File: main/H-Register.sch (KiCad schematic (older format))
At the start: 19 parts, among them U74 74LS245, U75 74LS173, U76 74LS173

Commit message: Replot main with symbols
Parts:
- renumbered D54 to D46, D55 to D47, D56 to D48, D57 to D49, D58 to D50, D59 to D51, D60 to D52, D61 to D53, R60 to R52, R61 to R53, R62 to R54, R63 to R55, R64 to R56, R65 to R57, R66 to R58, R67 to R59, U74 to U59, U75 to U60, U76 to U61
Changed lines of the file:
@@
 Sheet 16 26
 Title "H Register"
-Date "2019-11-13"
+Date "2019-11-17"
 Rev "v1.0"
 Comp "Christopher Milan"
@@
 AR Path="/5D9C73BD/5DA5FEC5" Ref="U?"  Part="1"
 AR Path="/5D9E8F33/5DA5FEC5" Ref="U?"  Part="1"
-AR Path="/5DA98D6D/5DA9A571/5DA5FEC5" Ref="U74"  Part="1"
-F 0 "U74" V 2996 2656 50  0000 R CNN
+AR Path="/5DA98D6D/5DA9A571/5DA5FEC5" Ref="U59"  Part="1"
+F 0 "U59" V 2996 2656 50  0000 R CNN
 F 1 "74LS245" V 2905 2656 50  0000 R CNN
 F 2 "" H 2950 3500 50  0001 C CNN
@@
 AR Path="/5D9C73BD/5DA5FEF2" Ref="U?"  Part="1"
 AR Path="/5D9E8F33/5DA5FEF2" Ref="U?"  Part="1"
-AR Path="/5DA98D6D/5DA9A571/5DA5FEF2" Ref="U76"  Part="1"
-F 0 "U76" V 7504 4444 50  0000 L CNN
+AR Path="/5DA98D6D/5DA9A571/5DA5FEF2" Ref="U61"  Part="1"
+F 0 "U61" V 7504 4444 50  0000 L CNN
 F 1 "74LS173" V 7595 4444 50  0000 L CNN
 F 2 "" H 7550 3500 50  0001 C CNN
@@
 AR Path="/5D9C73BD/5DA5FF1C" Ref="D?"  Part="1"
 AR Path="/5D9E8F33/5DA5FF1C" Ref="D?"  Part="1"
-AR Path="/5DA98D6D/5DA9A571/5DA5FF1C" Ref="D54"  Part="1"
-F 0 "D54" V 3539 5883 50  0000 R CNN
+AR Path="/5DA98D6D/5DA9A571/5DA5FF1C" Ref="D46"  Part="1"
+F 0 "D46" V 3539 5883 50  0000 R CNN
 F 1 "LED" V 3448 5883 50  0000 R CNN
 F 2 "" H 3500 6000 50  0001 C CNN
@@
 AR Path="/5D9C73BD/5DA5FF22" Ref="D?"  Part="1"
 AR Path="/5D9E8F33/5DA5FF22" Ref="D?"  Part="1"
-AR Path="/5DA98D6D/5DA9A571/5DA5FF22" Ref="D55"  Part="1"
-F 0 "D55" V 3889 5883 50  0000 R CNN
+AR Path="/5DA98D6D/5DA9A571/5DA5FF22" Ref="D47"  Part="1"
+F 0 "D47" V 3889 5883 50  0000 R CNN
 F 1 "LED" V 3798 5883 50  0000 R CNN
 F 2 "" H 3850 6000 50  0001 C CNN
@@
 AR Path="/5D9C73BD/5DA5FF28" Ref="D?"  Part="1"
 AR Path="/5D9E8F33/5DA5FF28" Ref="D?"  Part="1"
-AR Path="/5DA98D6D/5DA9A571/5DA5FF28" Ref="D56"  Part="1"
-F 0 "D56" V 4239 5883 50  0000 R CNN
+AR Path="/5DA98D6D/5DA9A571/5DA5FF28" Ref="D48"  Part="1"
+F 0 "D48" V 4239 5883 50  0000 R CNN
 F 1 "LED" V 4148 5883 50  0000 R CNN
 F 2 "" H 4200 6000 50  0001 C CNN
@@
 AR Path="/5D9C73BD/5DA5FF2E" Ref="D?"  Part="1"
 AR Path="/5D9E8F33/5DA5FF2E" Ref="D?"  Part="1"
-AR Path="/5DA98D6D/5DA9A571/5DA5FF2E" Ref="D57"  Part="1"
-F 0 "D57" V 4589 5883 50  0000 R CNN
+AR Path="/5DA98D6D/5DA9A571/5DA5FF2E" Ref="D49"  Part="1"
+F 0 "D49" V 4589 5883 50  0000 R CNN
 F 1 "LED" V 4498 5883 50  0000 R CNN
 F 2 "" H 4550 6000 50  0001 C CNN
@@
 AR Path="/5D9C73BD/5DA5FF34" Ref="D?"  Part="1"
 AR Path="/5D9E8F33/5DA5FF34" Ref="D?"  Part="1"
-AR Path="/5DA98D6D/5DA9A571/5DA5FF34" Ref="D58"  Part="1"
-F 0 "D58" V 4939 5883 50  0000 R CNN
+AR Path="/5DA98D6D/5DA9A571/5DA5FF34" Ref="D50"  Part="1"
+F 0 "D50" V 4939 5883 50  0000 R CNN
 F 1 "LED" V 4848 5883 50  0000 R CNN
 F 2 "" H 4900 6000 50  0001 C CNN
@@
 AR Path="/5D9C73BD/5DA5FF3A" Ref="D?"  Part="1"
 AR Path="/5D9E8F33/5DA5FF3A" Ref="D?"  Part="1"
-AR Path="/5DA98D6D/5DA9A571/5DA5FF3A" Ref="D59"  Part="1"
-F 0 "D59" V 5289 5883 50  0000 R CNN
+AR Path="/5DA98D6D/5DA9A571/5DA5FF3A" Ref="D51"  Part="1"
+F 0 "D51" V 5289 5883 50  0000 R CNN
 F 1 "LED" V 5198 5883 50  0000 R CNN
 F 2 "" H 5250 6000 50  0001 C CNN
@@
 AR Path="/5D9C73BD/5DA5FF40" Ref="D?"  Part="1"
 AR Path="/5D9E8F33/5DA5FF40" Ref="D?"  Part="1"
-AR Path="/5DA98D6D/5DA9A571/5DA5FF40" Ref="D60"  Part="1"
-F 0 "D60" V 5639 5883 50  0000 R CNN
+AR Path="/5DA98D6D/5DA9A571/5DA5FF40" Ref="D52"  Part="1"
+F 0 "D52" V 5639 5883 50  0000 R CNN
 F 1 "LED" V 5548 5883 50  0000 R CNN
 F 2 "" H 5600 6000 50  0001 C CNN
@@
 AR Path="/5D9C73BD/5DA5FF46" Ref="D?"  Part="1"
 AR Path="/5D9E8F33/5DA5FF46" Ref="D?"  Part="1"
-AR Path="/5DA98D6D/5DA9A571/5DA5FF46" Ref="D61"  Part="1"
-F 0 "D61" V 5989 5883 50  0000 R CNN
+AR Path="/5DA98D6D/5DA9A571/5DA5FF46" Ref="D53"  Part="1"
+F 0 "D53" V 5989 5883 50  0000 R CNN
 F 1 "LED" V 5898 5883 50  0000 R CNN
 F 2 "" H 5950 6000 50  0001 C CNN
@@
 AR Path="/5D9C73BD/5DA5FF62" Ref="R?"  Part="1"
 AR Path="/5D9E8F33/5DA5FF62" Ref="R?"  Part="1"
-AR Path="/5DA98D6D/5DA9A571/5DA5FF62" Ref="R60"  Part="1"
-F 0 "R60" H 3570 6596 50  0000 L CNN
+AR Path="/5DA98D6D/5DA9A571/5DA5FF62" Ref="R52"  Part="1"
+F 0 "R52" H 3570 6596 50  0000 L CNN
 F 1 "220" H 3570 6505 50  0000 L CNN
 F 2 "" V 3430 6550 50  0001 C CNN
@@
 AR Path="/5D9C73BD/5DA5FF68" Ref="R?"  Part="1"
 AR Path="/5D9E8F33/5DA5FF68" Ref="R?"  Part="1"
-AR Path="/5DA98D6D/5DA9A571/5DA5FF68" Ref="R61"  Part="1"
-F 0 "R61" H 3920 6596 50  0000 L CNN
+AR Path="/5DA98D6D/5DA9A571/5DA5FF68" Ref="R53"  Part="1"
+F 0 "R53" H 3920 6596 50  0000 L CNN
 F 1 "220" H 3920 6505 50  0000 L CNN
 F 2 "" V 3780 6550 50  0001 C CNN
@@
 AR Path="/5D9C73BD/5DA5FF6E" Ref="R?"  Part="1"
 AR Path="/5D9E8F33/5DA5FF6E" Ref="R?"  Part="1"
-AR Path="/5DA98D6D/5DA9A571/5DA5FF6E" Ref="R62"  Part="1"
-F 0 "R62" H 4270 6596 50  0000 L CNN
+AR Path="/5DA98D6D/5DA9A571/5DA5FF6E" Ref="R54"  Part="1"
+F 0 "R54" H 4270 6596 50  0000 L CNN
 F 1 "220" H 4270 6505 50  0000 L CNN
 F 2 "" V 4130 6550 50  0001 C CNN
@@
 AR Path="/5D9C73BD/5DA5FF74" Ref="R?"  Part="1"
 AR Path="/5D9E8F33/5DA5FF74" Ref="R?"  Part="1"
-AR Path="/5DA98D6D/5DA9A571/5DA5FF74" Ref="R63"  Part="1"
-F 0 "R63" H 4620 6596 50  0000 L CNN
+AR Path="/5DA98D6D/5DA9A571/5DA5FF74" Ref="R55"  Part="1"
+F 0 "R55" H 4620 6596 50  0000 L CNN
 F 1 "220" H 4620 6505 50  0000 L CNN
 F 2 "" V 4480 6550 50  0001 C CNN
@@
 AR Path="/5D9C73BD/5DA5FF7A" Ref="R?"  Part="1"
 AR Path="/5D9E8F33/5DA5FF7A" Ref="R?"  Part="1"
-AR Path="/5DA98D6D/5DA9A571/5DA5FF7A" Ref="R64"  Part="1"
-F 0 "R64" H 4970 6596 50  0000 L CNN
+AR Path="/5DA98D6D/5DA9A571/5DA5FF7A" Ref="R56"  Part="1"
+F 0 "R56" H 4970 6596 50  0000 L CNN
 F 1 "220" H 4970 6505 50  0000 L CNN
 F 2 "" V 4830 6550 50  0001 C CNN
@@
 AR Path="/5D9C73BD/5DA5FF80" Ref="R?"  Part="1"
 AR Path="/5D9E8F33/5DA5FF80" Ref="R?"  Part="1"
-AR Path="/5DA98D6D/5DA9A571/5DA5FF80" Ref="R65"  Part="1"
-F 0 "R65" H 5320 6596 50  0000 L CNN
+AR Path="/5DA98D6D/5DA9A571/5DA5FF80" Ref="R57"  Part="1"
+F 0 "R57" H 5320 6596 50  0000 L CNN
 F 1 "220" H 5320 6505 50  0000 L CNN
 F 2 "" V 5180 6550 50  0001 C CNN
@@
 AR Path="/5D9C73BD/5DA5FF86" Ref="R?"  Part="1"
 AR Path="/5D9E8F33/5DA5FF86" Ref="R?"  Part="1"
-AR Path="/5DA98D6D/5DA9A571/5DA5FF86" Ref="R66"  Part="1"
-F 0 "R66" H 5670 6596 50  0000 L CNN
+AR Path="/5DA98D6D/5DA9A571/5DA5FF86" Ref="R58"  Part="1"
+F 0 "R58" H 5670 6596 50  0000 L CNN
 F 1 "220" H 5670 6505 50  0000 L CNN
 F 2 "" V 5530 6550 50  0001 C CNN
@@
 AR Path="/5D9C73BD/5DA5FF8C" Ref="R?"  Part="1"
 AR Path="/5D9E8F33/5DA5FF8C" Ref="R?"  Part="1"
-AR Path="/5DA98D6D/5DA9A571/5DA5FF8C" Ref="R67"  Part="1"
-F 0 "R67" H 6020 6596 50  0000 L CNN
+AR Path="/5DA98D6D/5DA9A571/5DA5FF8C" Ref="R59"  Part="1"
+F 0 "R59" H 6020 6596 50  0000 L CNN
 F 1 "220" H 6020 6505 50  0000 L CNN
 F 2 "" V 5880 6550 50  0001 C CNN
@@
 AR Path="/5D9C73BD/5DA5FFDD" Ref="U?"  Part="1"
 AR Path="/5D9E8F33/5DA5FFDD" Ref="U?"  Part="1"
-AR Path="/5DA98D6D/5DA9A571/5DA5FFDD" Ref="U75"  Part="1"
-F 0 "U75" V 5254 4444 50  0000 L CNN
+AR Path="/5DA98D6D/5DA9A571/5DA5FFDD" Ref="U60"  Part="1"
+F 0 "U60" V 5254 4444 50  0000 L CNN
 F 1 "74LS173" V 5345 4444 50  0000 L CNN
 F 2 "" H 5300 3500 50  0001 C CNN

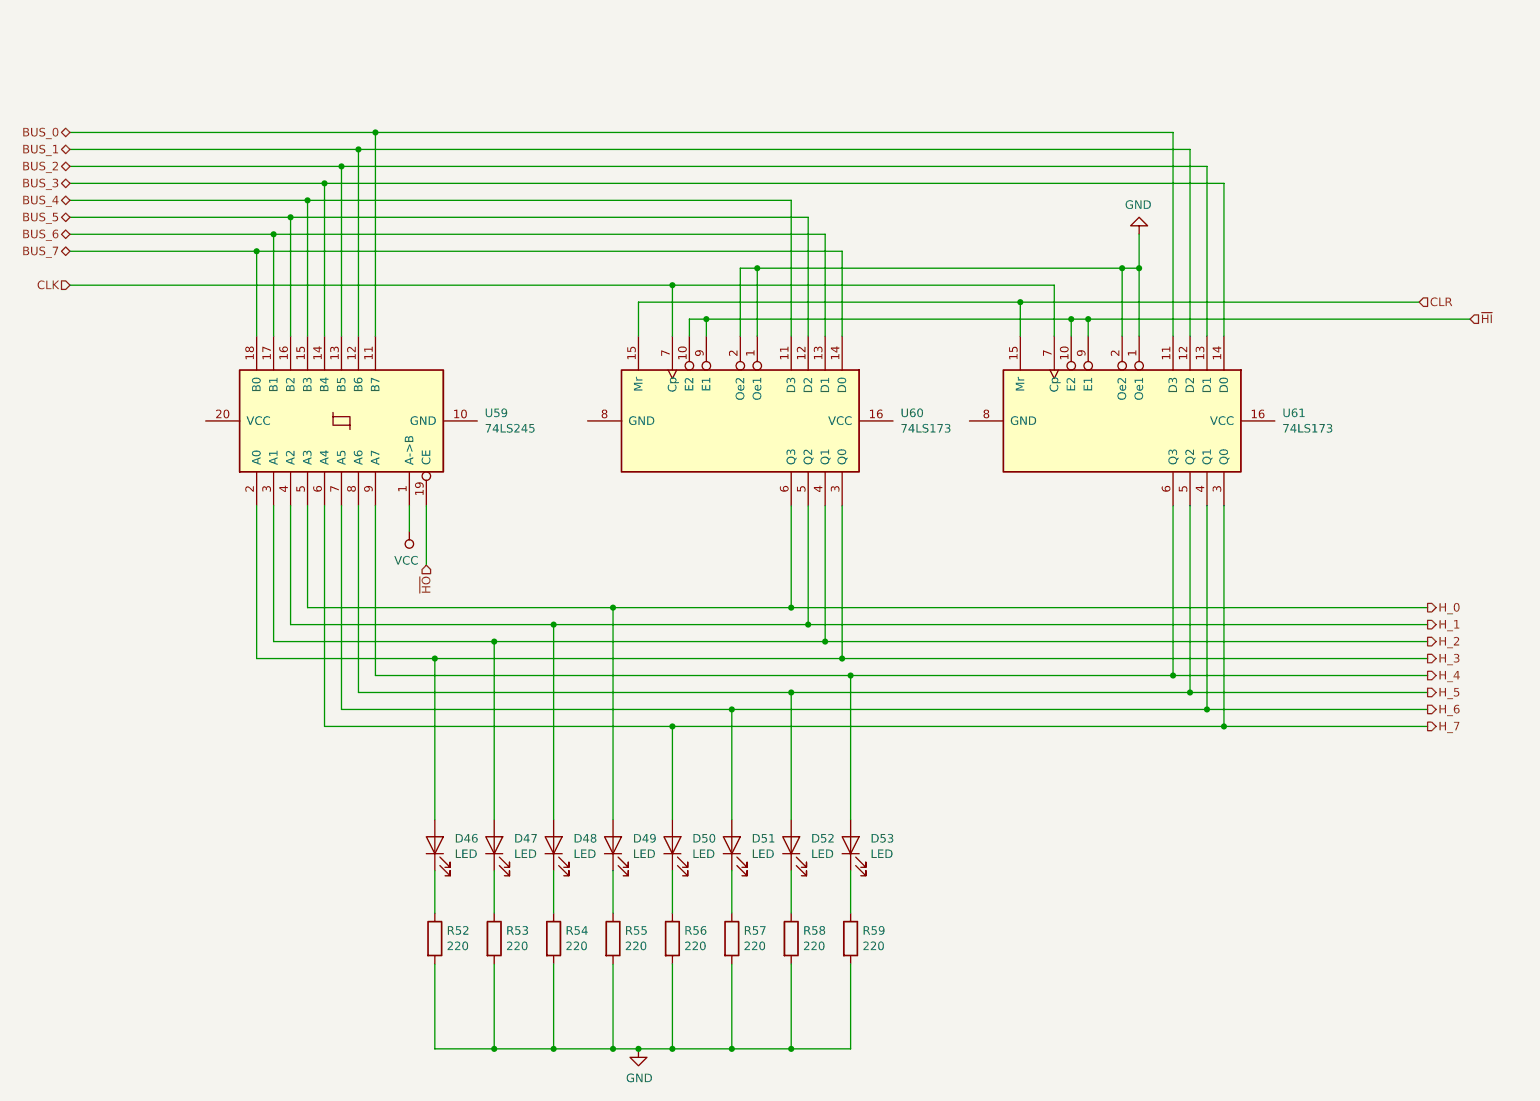
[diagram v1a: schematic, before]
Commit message: Switch to using 74LS377 in place of two 74LS173
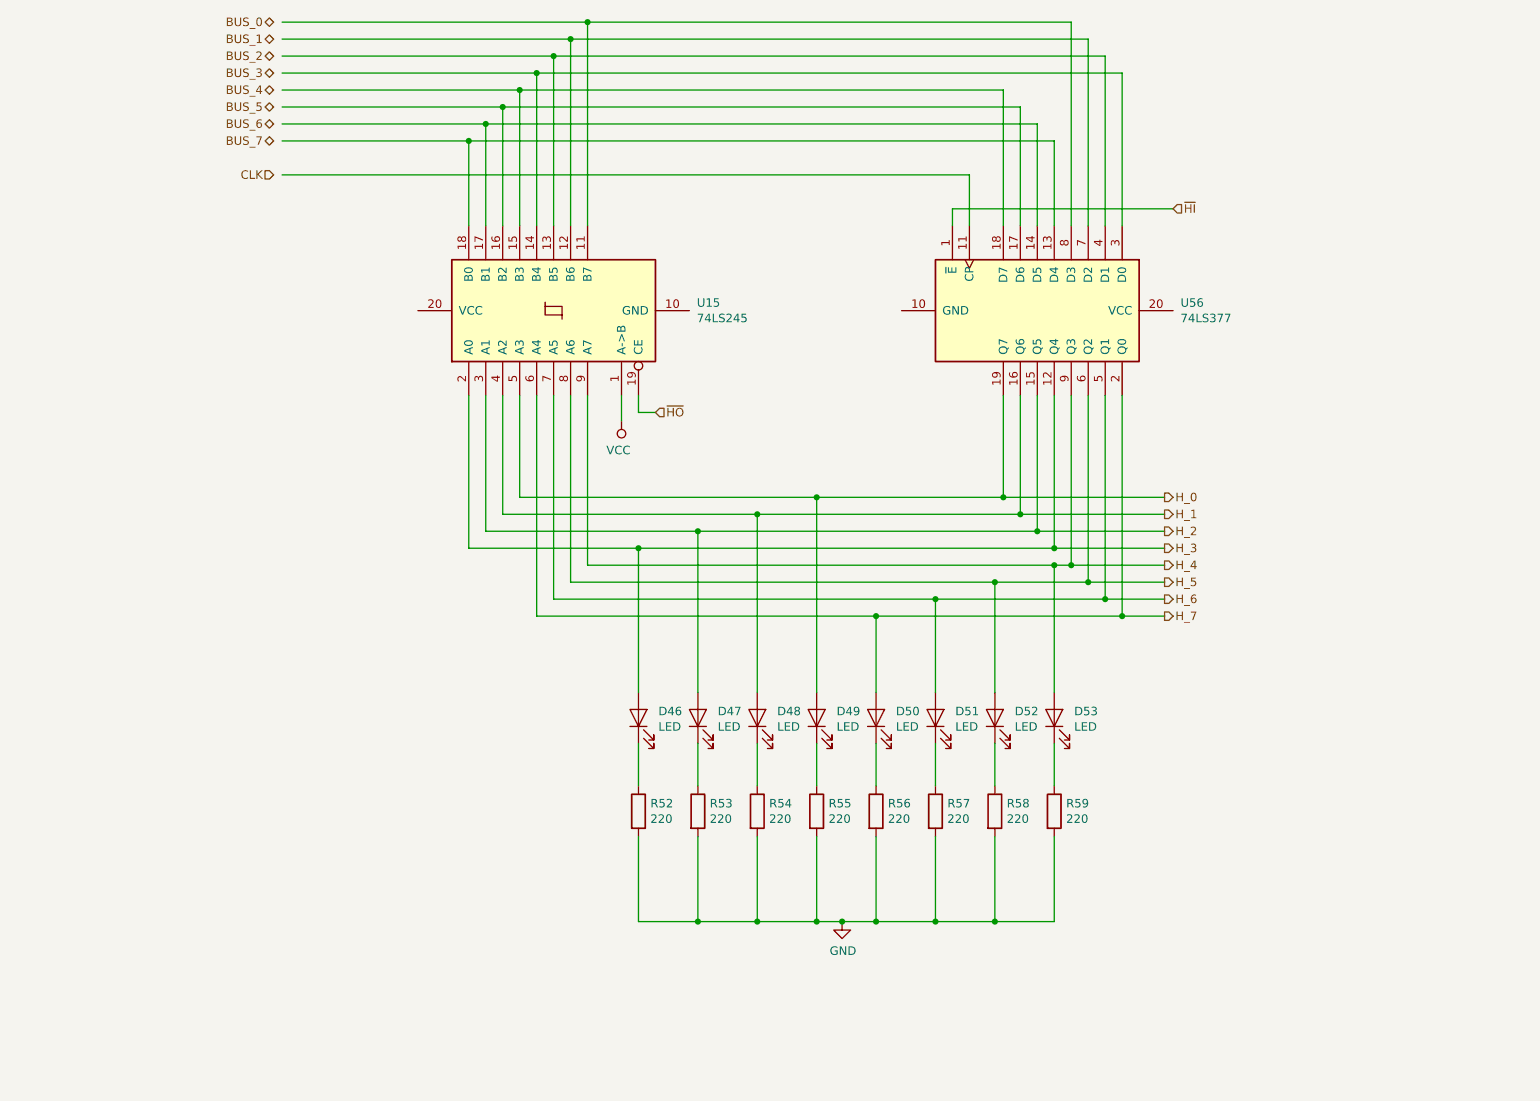
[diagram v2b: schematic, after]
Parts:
- removed U59: 74LS245, symbol 74xx:74LS245
- removed U60, U61: 74LS173, symbol 74xx:74LS173
- added U15: 74LS245, symbol 74xx:74LS245
- added U56: 74LS377, symbol 74xx:74LS377
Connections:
- net labels removed: CLR
- wire segments 130 -> 111
